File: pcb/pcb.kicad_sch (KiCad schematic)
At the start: 68 parts, among them J1 USB_C_Receptacle_USB2.0, SW1 SW_Push, SW2 SW_Push, U1 SRV05-4, U10 RP2040, U11 W25Q128JVS, U2 XC6206P332MR, U3 DRV5056A3xDBZxQ1, U4 DRV5056A3xDBZxQ1, U5 DRV5056A3xDBZxQ1, U6 74AHCT1G125, U7 74AHCT1G125, U8 74AHCT1G125, U9 74AHCT1G125, Y1 12MHz

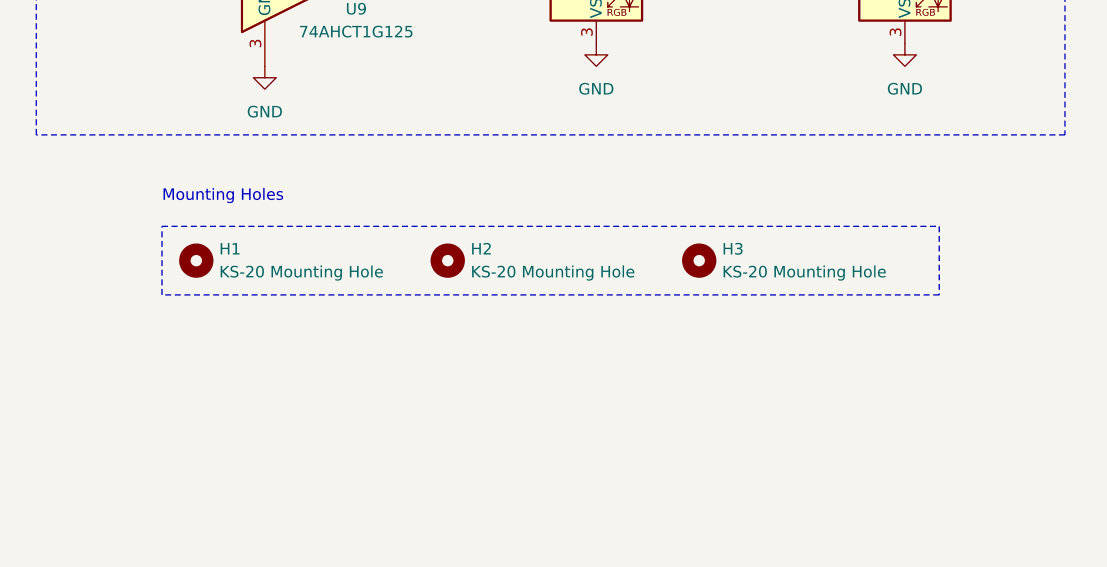
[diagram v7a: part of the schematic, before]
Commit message: feat: add m2 screw holes the footprint already takes the 4mm width of the standoffs into account, so should be OK as long as I position it correctly in CAD.
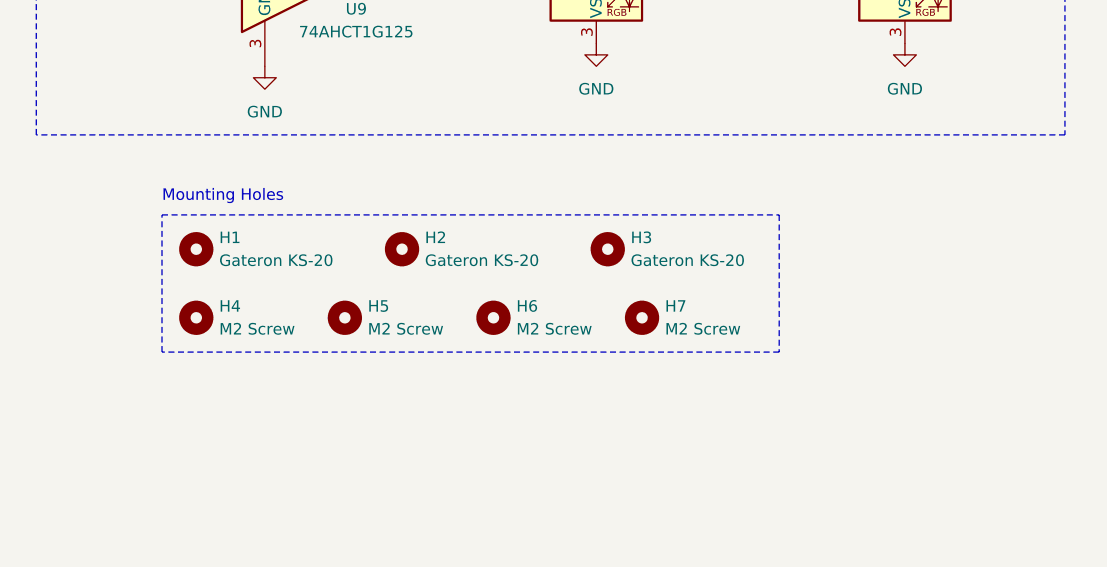
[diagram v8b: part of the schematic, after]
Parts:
- added H4, H5, H6, H7: M2 Screw, MountingHole:MountingHole_2.2mm_M2, symbol Mechanical:MountingHole
- H1, H2, H3: value KS-20 Mounting Hole -> Gateron KS-20
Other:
- moved on the sheet: H1, H2, H3
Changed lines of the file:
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@@
     (stroke (width 0) (type default))
   )
-  (rectangle (start 175.26 170.18) (end 261.62 177.8)
+  (rectangle (start 175.26 168.91) (end 243.84 184.15)
     (stroke (width 0) (type dash))
     (fill (type none))
@@
     )
   )
-  (symbol (lib_id "Mechanical:MountingHole") (at 207.01 173.99 0) (unit 1)
+  (symbol (lib_id "Mechanical:MountingHole") (at 201.93 172.72 0) (unit 1)
     (in_bom yes) (on_board yes) (dnp no) (fields_autoplaced)
-    (property "Reference" "H2" (at 209.55 172.72 0)
+    (property "Reference" "H2" (at 204.47 171.45 0)
       (effects (font (size 1.27 1.27)) (justify left))
     )
-    (property "Value" "KS-20 Mounting Hole" (at 209.55 175.26 0)
+    (property "Value" "Gateron KS-20" (at 204.47 173.99 0)
       (effects (font (size 1.27 1.27)) (justify left))
     )
-    (property "Footprint" "Harukapad:MX-1U-NoPins" (at 207.01 173.99 0)
+    (property "Footprint" "Harukapad:MX-1U-NoPins" (at 201.93 172.72 0)
       (effects (font (size 1.27 1.27)) hide)
     )
-    (property "Datasheet" "~" (at 207.01 173.99 0)
+    (property "Datasheet" "~" (at 201.93 172.72 0)
       (effects (font (size 1.27 1.27)) hide)
     )
@@
     )
   )
+  (symbol (lib_id "Mechanical:MountingHole") (at 195.58 180.34 0) (unit 1)
+    (in_bom yes) (on_board yes) (dnp no) (fields_autoplaced)
+    (property "Reference" "H5" (at 198.12 179.07 0)
+      (effects (font (size 1.27 1.27)) (justify left))
+    )
+    (property "Value" "M2 Screw" (at 198.12 181.61 0)
+      (effects (font (size 1.27 1.27)) (justify left))
+    )
+    (property "Footprint" "MountingHole:MountingHole_2.2mm_M2" (at 195.58 180.34 0)
+      (effects (font (size 1.27 1.27)) hide)
+    )
+    (property "Datasheet" "~" (at 195.58 180.34 0)
+      (effects (font (size 1.27 1.27)) hide)
+    )
+    (instances
+      (project "pcb"
+        (path "/fe0c1c23-b294-4653-a8db-85682224ef67"
+          (reference "H5") (unit 1)
+        )
+      )
+    )
+  )
   (symbol (lib_id "power:+3V3") (at 130.81 152.4 0) (unit 1)
     (in_bom yes) (on_board yes) (dnp no) (fields_autoplaced)
@@
     )
   )
-  (symbol (lib_id "Mechanical:MountingHole") (at 179.07 173.99 0) (unit 1)
+  (symbol (lib_id "Mechanical:MountingHole") (at 179.07 172.72 0) (unit 1)
     (in_bom yes) (on_board yes) (dnp no) (fields_autoplaced)
-    (property "Reference" "H1" (at 181.61 172.72 0)
+    (property "Reference" "H1" (at 181.61 171.45 0)
       (effects (font (size 1.27 1.27)) (justify left))
     )
-    (property "Value" "KS-20 Mounting Hole" (at 181.61 175.26 0)
+    (property "Value" "Gateron KS-20" (at 181.61 173.99 0)
       (effects (font (size 1.27 1.27)) (justify left))
     )
-    (property "Footprint" "Harukapad:MX-1U-NoPins" (at 179.07 173.99 0)
+    (property "Footprint" "Harukapad:MX-1U-NoPins" (at 179.07 172.72 0)
       (effects (font (size 1.27 1.27)) hide)
     )
-    (property "Datasheet" "~" (at 179.07 173.99 0)
+    (property "Datasheet" "~" (at 179.07 172.72 0)
       (effects (font (size 1.27 1.27)) hide)
     )
@@
     )
   )
+  (symbol (lib_id "Mechanical:MountingHole") (at 212.09 180.34 0) (unit 1)
+    (in_bom yes) (on_board yes) (dnp no) (fields_autoplaced)
+    (property "Reference" "H6" (at 214.63 179.07 0)
+      (effects (font (size 1.27 1.27)) (justify left))
+    )
+    (property "Value" "M2 Screw" (at 214.63 181.61 0)
+      (effects (font (size 1.27 1.27)) (justify left))
+    )
+    (property "Footprint" "MountingHole:MountingHole_2.2mm_M2" (at 212.09 180.34 0)
+      (effects (font (size 1.27 1.27)) hide)
+    )
+    (property "Datasheet" "~" (at 212.09 180.34 0)
+      (effects (font (size 1.27 1.27)) hide)
+    )
+    (instances
+      (project "pcb"
+        (path "/fe0c1c23-b294-4653-a8db-85682224ef67"
+          (reference "H6") (unit 1)
+        )
+      )
+    )
+  )
   (symbol (lib_id "Device:C_Small") (at 228.6 31.75 90) (unit 1)
     (in_bom yes) (on_board yes) (dnp no) (fields_autoplaced)
@@
     )
   )
-  (symbol (lib_id "Mechanical:MountingHole") (at 234.95 173.99 0) (unit 1)
+  (symbol (lib_id "Mechanical:MountingHole") (at 224.79 172.72 0) (unit 1)
     (in_bom yes) (on_board yes) (dnp no) (fields_autoplaced)
-    (property "Reference" "H3" (at 237.49 172.72 0)
+    (property "Reference" "H3" (at 227.33 171.45 0)
       (effects (font (size 1.27 1.27)) (justify left))
     )
-    (property "Value" "KS-20 Mounting Hole" (at 237.49 175.26 0)
+    (property "Value" "Gateron KS-20" (at 227.33 173.99 0)
       (effects (font (size 1.27 1.27)) (justify left))
     )
-    (property "Footprint" "Harukapad:MX-1U-NoPins" (at 234.95 173.99 0)
+    (property "Footprint" "Harukapad:MX-1U-NoPins" (at 224.79 172.72 0)
       (effects (font (size 1.27 1.27)) hide)
     )
-    (property "Datasheet" "~" (at 234.95 173.99 0)
+    (property "Datasheet" "~" (at 224.79 172.72 0)
       (effects (font (size 1.27 1.27)) hide)
     )
@@
     )
   )
+  (symbol (lib_id "Mechanical:MountingHole") (at 228.6 180.34 0) (unit 1)
+    (in_bom yes) (on_board yes) (dnp no) (fields_autoplaced)
+    (property "Reference" "H7" (at 231.14 179.07 0)
+      (effects (font (size 1.27 1.27)) (justify left))
+    )
+    (property "Value" "M2 Screw" (at 231.14 181.61 0)
+      (effects (font (size 1.27 1.27)) (justify left))
+    )
+    (property "Footprint" "MountingHole:MountingHole_2.2mm_M2" (at 228.6 180.34 0)
+      (effects (font (size 1.27 1.27)) hide)
+    )
+    (property "Datasheet" "~" (at 228.6 180.34 0)
+      (effects (font (size 1.27 1.27)) hide)
+    )
+    (instances
+      (project "pcb"
+        (path "/fe0c1c23-b294-4653-a8db-85682224ef67"
+          (reference "H7") (unit 1)
+        )
+      )
+    )
+  )
   (symbol (lib_id "74xGxx:74AHCT1G125") (at 269.24 91.44 0) (unit 1)
     (in_bom yes) (on_board yes) (dnp no)
@@
         )
       )
+    )
+  )
+  (symbol (lib_id "Mechanical:MountingHole") (at 179.07 180.34 0) (unit 1)
+    (in_bom yes) (on_board yes) (dnp no) (fields_autoplaced)
+    (property "Reference" "H4" (at 181.61 179.07 0)
+      (effects (font (size 1.27 1.27)) (justify left))
+    )
+    (property "Value" "M2 Screw" (at 181.61 181.61 0)
+      (effects (font (size 1.27 1.27)) (justify left))
+    )
+    (property "Footprint" "MountingHole:MountingHole_2.2mm_M2" (at 179.07 180.34 0)
+      (effects (font (size 1.27 1.27)) hide)
+    )
+    (property "Datasheet" "~" (at 179.07 180.34 0)
+      (effects (font (size 1.27 1.27)) hide)
+    )
+    (instances
+      (project "pcb"
+        (path "/fe0c1c23-b294-4653-a8db-85682224ef67"
+          (reference "H4") (unit 1)
+        )
+      )
